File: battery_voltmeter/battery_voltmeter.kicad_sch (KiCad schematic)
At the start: 12 parts, among them J1 Conn_02x08_Odd_Even, J2 USB_B_Micro, U1 SP420281N, U2 ATSAMD21E18A-A, U3 L7805, U4 AP2112K-3.3

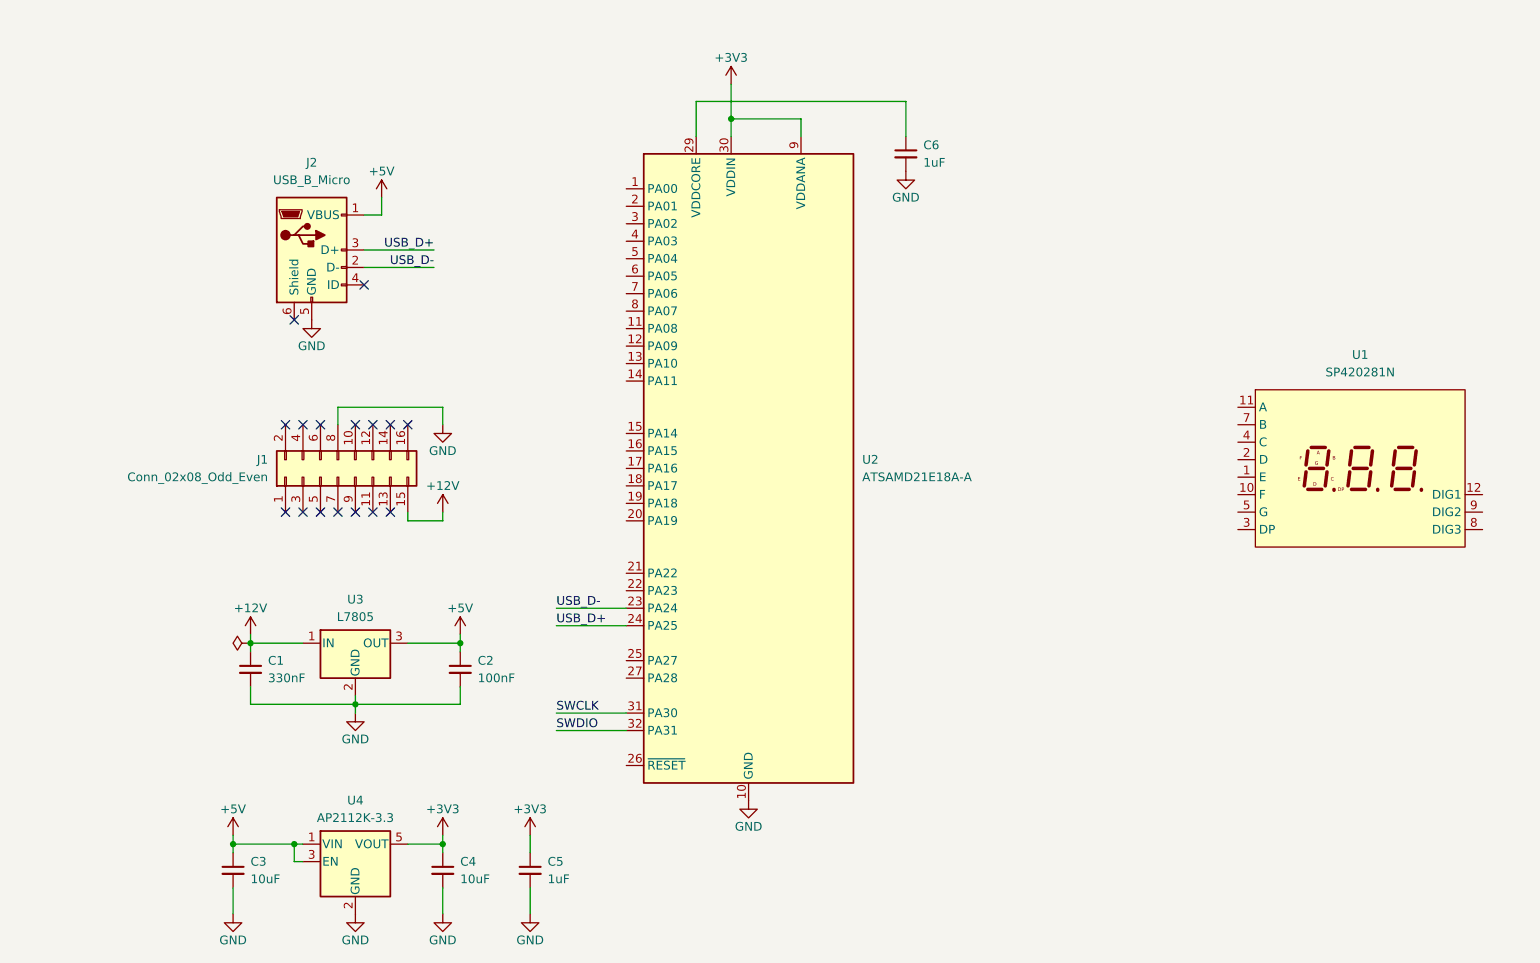
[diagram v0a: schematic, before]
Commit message: WIP battery voltmeter module: part 2
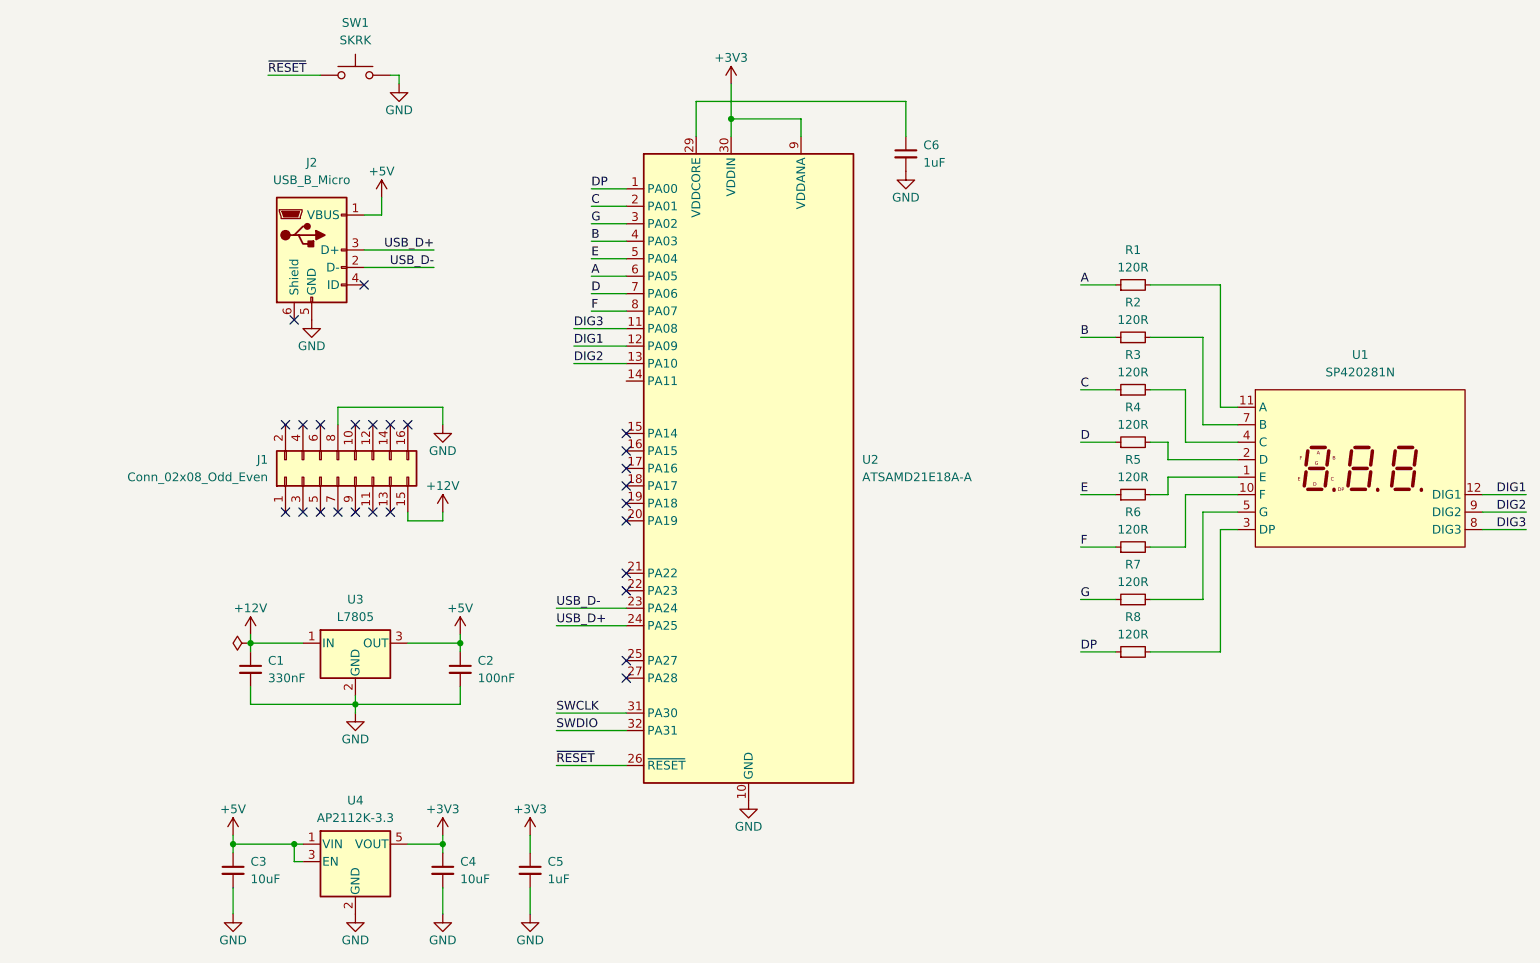
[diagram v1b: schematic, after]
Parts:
- added R1, R2, R3, R4, R5, R6, R7, R8: 120R, Resistor_SMD:R_0603_1608Metric_Pad0.98x0.95mm_HandSolder, symbol Device:R_Small
- added SW1: SKRK, Button_Switch_SMD:SW_Push_SPST_NO_Alps_SKRK, symbol Switch:SW_Push
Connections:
- net GND: now also SW1.2
- net at U1.1 (E): now also R5.2
- net at U1.10 (F): now also R6.2
- net at U1.11 (A): now also R1.2
- net DIG1: now reaches U1.12 (DIG1)
- net DIG1: now also U2.12 (PA09)
- net at U1.2 (D): now also R4.2
- net at U1.3 (DP): now also R8.2
- net at U1.4 (C): now also R3.2
- net at U1.5 (G): now also R7.2
- net at U1.7 (B): now also R2.2
- net DIG3: now reaches U1.8 (DIG3)
- net DIG3: now also U2.11 (PA08)
- net DIG2: now reaches U1.9 (DIG2)
- net DIG2: now also U2.13 (PA10)
- net DP: now reaches U2.1 (PA00)
- net DP: now also R8.1
- net C: now reaches U2.2 (PA01)
- net C: now also R3.1
- net ~{RESET}: now reaches U2.26 (~{RESET})
- net ~{RESET}: now also SW1.1
- net G: now reaches U2.3 (PA02)
- net G: now also R7.1
- net B: now reaches U2.4 (PA03)
- net B: now also R2.1
- net E: now reaches U2.5 (PA04)
- net E: now also R5.1
- net A: now reaches U2.6 (PA05)
- net A: now also R1.1
- net D: now reaches U2.7 (PA06)
- net D: now also R4.1
- net F: now reaches U2.8 (PA07)
- net F: now also R6.1
- no-connect marks 16 -> 26

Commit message: WIP battery voltmeter module: part 3
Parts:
- added TP1: +3V3, TestPoint:TestPoint_Pad_D1.0mm, symbol Connector:TestPoint
- added TP2: SWCLK, TestPoint:TestPoint_Pad_D1.0mm, symbol Connector:TestPoint
- added TP3: SWDIO, TestPoint:TestPoint_Pad_D1.0mm, symbol Connector:TestPoint
- added TP4: GND, TestPoint:TestPoint_Pad_D1.0mm, symbol Connector:TestPoint
- U3: LCSC (none) -> C58069
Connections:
- net +3V3: now also TP1.1
- net GND: now also TP4.1
- net SWCLK: now also TP2.1
- net SWDIO: now also TP3.1
- net V_MEASURE: now reaches U2.14 (PA11)

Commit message: Finish battery voltmeter module
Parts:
- added R9: 22R, Resistor_SMD:R_0603_1608Metric_Pad0.98x0.95mm_HandSolder, symbol Device:R_Small
- added RV1: 5k, Potentiometer_THT:Potentiometer_Bourns_3296W_Vertical, symbol Device:R_Potentiometer_Small
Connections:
- net +12V: now also RV1.3
- net GND: now also J2.6 (Shield), R9.2
- net V_MEASURE: now also RV1.2
- new net: R9.1, RV1.1
- no-connect marks 26 -> 25
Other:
- moved on the sheet: C1, C2, C3, C4, C5, J1, J2, SW1, U3, U4

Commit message: Fix component selection issue, add battery voltmeter firmware
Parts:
- R9: value 22R -> 10k; LCSC C23345 -> C25804
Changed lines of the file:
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@@
 			)
 		)
-		(property "Value" "22R"
+		(property "Value" "10k"
 			(at 223.52 68.5799 0)
 			(effects
@@
 			)
 		)
-		(property "LCSC" "C23345"
+		(property "LCSC" "C25804"
 			(at 220.98 67.31 0)
 			(effects

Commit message: Fix serious voltage divider issue
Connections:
- net +12V: now also R9.1; no longer RV1.3
- net GND: now also RV1.1; no longer R9.2
- new net: R9.2, RV1.3
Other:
- moved on the sheet: R9, RV1
